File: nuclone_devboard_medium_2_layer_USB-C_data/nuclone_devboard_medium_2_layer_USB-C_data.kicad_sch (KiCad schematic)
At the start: 39 parts, among them J1 JTAG_2X05, J2 TYPE-C-31-M-12, J3 nuclone_medium_left, J4 nuclone_medium_right, SW1 RESET, SW2 Bootloader, U1 MCP1702-3.3V, U2 TPESD0504C6

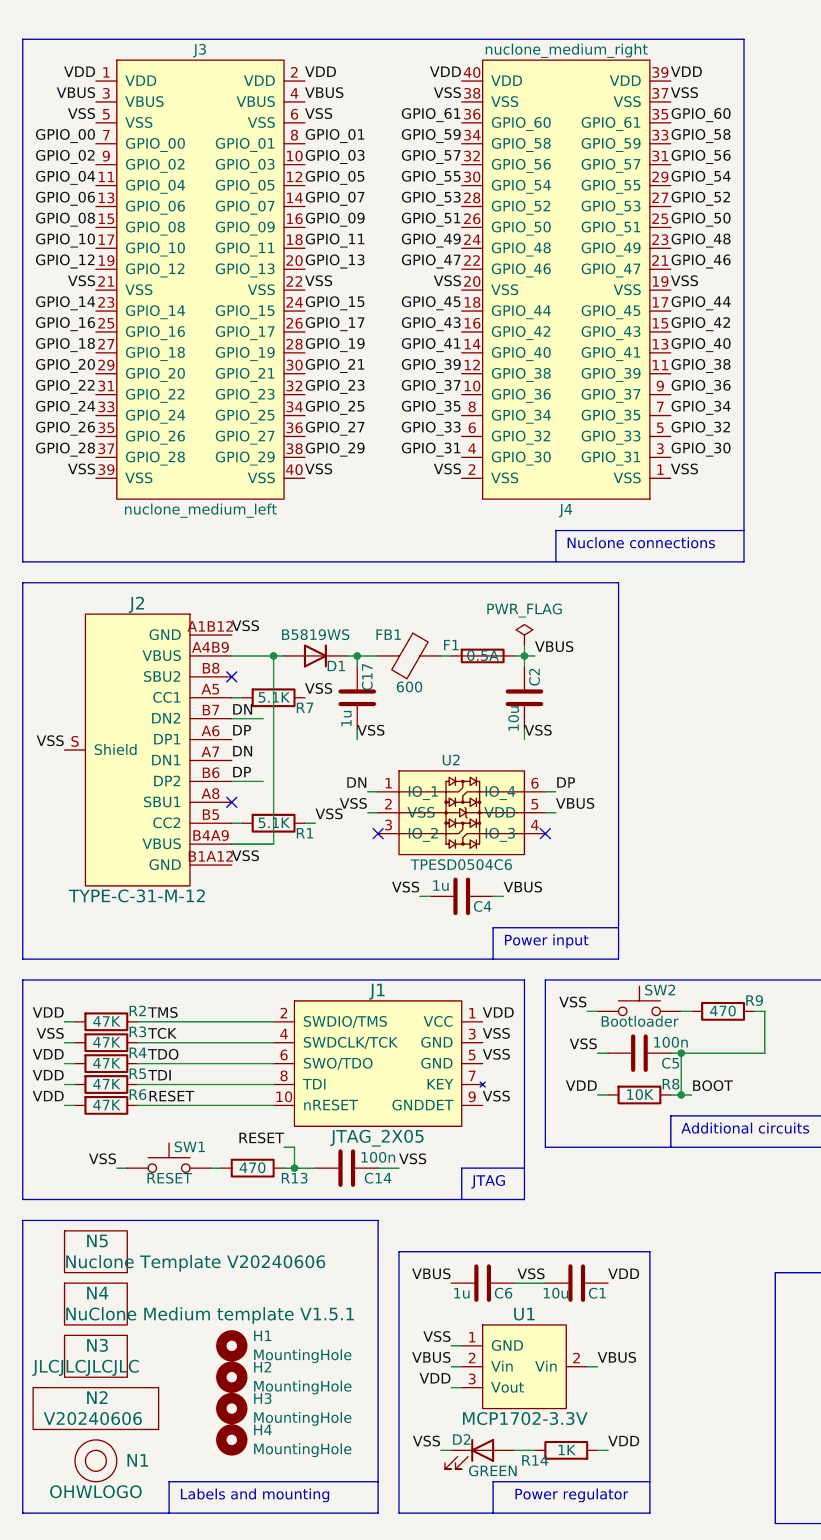
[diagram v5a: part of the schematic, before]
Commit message: updated using board outline footprint
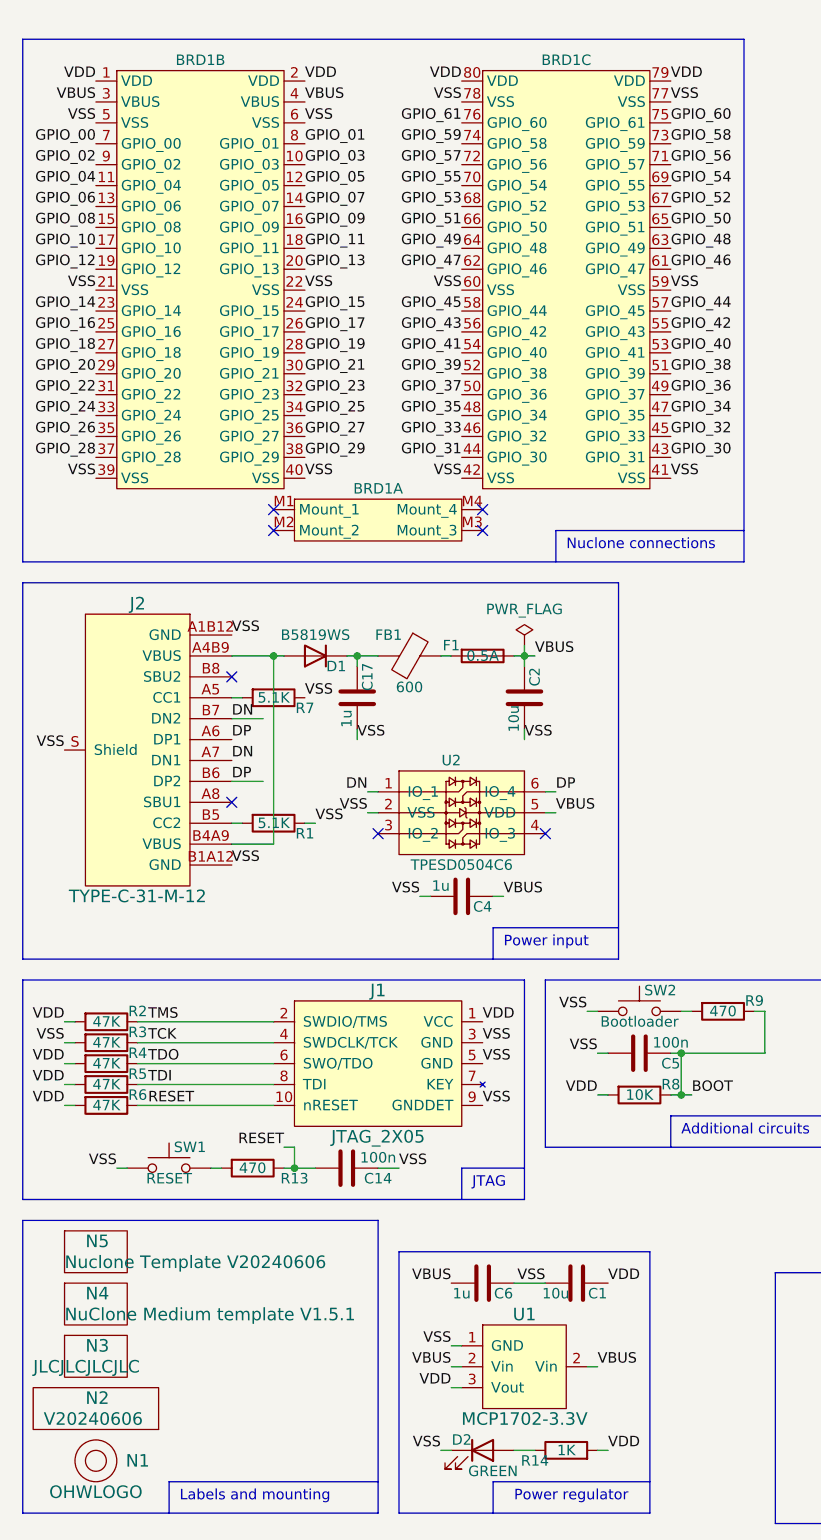
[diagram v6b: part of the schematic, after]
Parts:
- removed H1, H2, H3, H4: MountingHole, SquantorPcbOutline:MountingHole_3.2mm_M3_Pad_Via, symbol Mechanical:MountingHole
- removed J3: nuclone_medium_left, SquantorConnectorsNamed:nuclone_medium_left_stacked, symbol SquantorConnectorsNamed:nuclone_medium_left
- removed J4: nuclone_medium_right, SquantorConnectorsNamed:nuclone_medium_right_stacked, symbol SquantorConnectorsNamed:nuclone_medium_right
- added BRD1: ~, SquantorNuclone:Devboard_medium_generic, symbol SquantorNuclone:Medium_development_generic
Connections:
- net GPIO_00: now also BRD1.7 (GPIO_00)
- net GPIO_01: now also BRD1.8 (GPIO_01)
- net GPIO_02: now also BRD1.9 (GPIO_02)
- net GPIO_03: now also BRD1.10 (GPIO_03)
- net GPIO_04: now also BRD1.11 (GPIO_04)
- net GPIO_05: now also BRD1.12 (GPIO_05)
- net GPIO_06: now also BRD1.13 (GPIO_06)
- net GPIO_07: now also BRD1.14 (GPIO_07)
- net GPIO_08: now also BRD1.15 (GPIO_08)
- net GPIO_09: now also BRD1.16 (GPIO_09)
- net GPIO_10: now also BRD1.17 (GPIO_10)
- net GPIO_11: now also BRD1.18 (GPIO_11)
- net GPIO_12: now also BRD1.19 (GPIO_12)
- net GPIO_13: now also BRD1.20 (GPIO_13)
- net GPIO_14: now also BRD1.23 (GPIO_14)
- net GPIO_15: now also BRD1.24 (GPIO_15)
- net GPIO_16: now also BRD1.25 (GPIO_16)
- net GPIO_17: now also BRD1.26 (GPIO_17)
- net GPIO_18: now also BRD1.27 (GPIO_18)
- net GPIO_19: now also BRD1.28 (GPIO_19)
- net GPIO_20: now also BRD1.29 (GPIO_20)
- net GPIO_21: now also BRD1.30 (GPIO_21)
- net GPIO_22: now also BRD1.31 (GPIO_22)
- net GPIO_23: now also BRD1.32 (GPIO_23)
- net GPIO_24: now also BRD1.33 (GPIO_24)
- net GPIO_25: now also BRD1.34 (GPIO_25)
- net GPIO_26: now also BRD1.35 (GPIO_26)
- net GPIO_27: now also BRD1.36 (GPIO_27)
- net GPIO_28: now also BRD1.37 (GPIO_28)
- net GPIO_29: now also BRD1.38 (GPIO_29)
- net GPIO_30: now also BRD1.43 (GPIO_31)
- net GPIO_31: now also BRD1.44 (GPIO_30)
- net GPIO_32: now also BRD1.45 (GPIO_33)
- net GPIO_33: now also BRD1.46 (GPIO_32)
- net GPIO_34: now also BRD1.47 (GPIO_35)
- net GPIO_35: now also BRD1.48 (GPIO_34)
- net GPIO_36: now also BRD1.49 (GPIO_37)
- net GPIO_37: now also BRD1.50 (GPIO_36)
- net GPIO_38: now also BRD1.51 (GPIO_39)
- net GPIO_39: now also BRD1.52 (GPIO_38)
- net GPIO_40: now also BRD1.53 (GPIO_41)
- net GPIO_41: now also BRD1.54 (GPIO_40)
- net GPIO_42: now also BRD1.55 (GPIO_43)
- net GPIO_43: now also BRD1.56 (GPIO_42)
- net GPIO_44: now also BRD1.57 (GPIO_45)
- net GPIO_45: now also BRD1.58 (GPIO_44)
- net GPIO_46: now also BRD1.61 (GPIO_47)
- net GPIO_47: now also BRD1.62 (GPIO_46)
- net GPIO_48: now also BRD1.63 (GPIO_49)
- net GPIO_49: now also BRD1.64 (GPIO_48)
- net GPIO_50: now also BRD1.65 (GPIO_51)
- net GPIO_51: now also BRD1.66 (GPIO_50)
- net GPIO_52: now also BRD1.67 (GPIO_53)
- net GPIO_53: now also BRD1.68 (GPIO_52)
- net GPIO_54: now also BRD1.69 (GPIO_55)
- net GPIO_55: now also BRD1.70 (GPIO_54)
- net GPIO_56: now also BRD1.71 (GPIO_57)
- net GPIO_57: now also BRD1.72 (GPIO_56)
- net GPIO_58: now also BRD1.73 (GPIO_59)
- net GPIO_59: now also BRD1.74 (GPIO_58)
- net GPIO_60: now also BRD1.75 (GPIO_61)
- net GPIO_61: now also BRD1.76 (GPIO_60)
- net VBUS: now also BRD1.3 (VBUS), BRD1.4 (VBUS)
- net VDD: now also BRD1.1 (VDD), BRD1.2 (VDD), BRD1.79 (VDD), BRD1.80 (VDD)
- net VSS: now also BRD1.21 (VSS), BRD1.22 (VSS), BRD1.39 (VSS), BRD1.40 (VSS), BRD1.41 (VSS), BRD1.42 (VSS), BRD1.5 (VSS), BRD1.59 (VSS), BRD1.6 (VSS), BRD1.60 (VSS), BRD1.77 (VSS), BRD1.78 (VSS)
- no-connect marks 4 -> 8
